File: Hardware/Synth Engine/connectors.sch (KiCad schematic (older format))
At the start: 8 parts, among them J10 Conn_01x13, J11 Conn_01x13, J13 Conn_01x05, J14 Conn_01x05, J15 Conn_01x05, J16 Conn_01x05, J8 Conn_01x13, J9 Conn_01x13

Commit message: fix LFO connector schem
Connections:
- net labels added: lfo_in_1, lfo_in_2, lfo_in_3, lfo_in_4, lfo_out_1, lfo_out_2, lfo_out_3, lfo_out_4
- wire segments 96 -> 104
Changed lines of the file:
@@
 	-1   0    0    -1
 $EndComp
+Text Label 3800 1450 0    60   ~ 0
+lfo_in_1
+Text Label 3800 1550 0    60   ~ 0
+lfo_out_1
+Text Label 3800 2150 0    60   ~ 0
+lfo_in_2
+Text Label 3800 2250 0    60   ~ 0
+lfo_out_2
+Text Label 3800 2800 0    60   ~ 0
+lfo_in_3
+Text Label 3800 2900 0    60   ~ 0
+lfo_out_3
+Text Label 3800 3450 0    60   ~ 0
+lfo_in_4
+Text Label 3800 3550 0    60   ~ 0
+lfo_out_4
+Text Label 8050 5650 2    60   ~ 0
+lfo_in_1
+Text Label 8050 5750 2    60   ~ 0
+lfo_out_1
+Text Label 8050 5850 2    60   ~ 0
+lfo_in_2
+Text Label 8050 5950 2    60   ~ 0
+lfo_out_2
+Text Label 8050 6050 2    60   ~ 0
+lfo_in_3
+Text Label 8050 6150 2    60   ~ 0
+lfo_out_3
+Text Label 8050 6250 2    60   ~ 0
+lfo_in_4
+Text Label 8050 6350 2    60   ~ 0
+lfo_out_4
+Text HLabel 8250 5650 2    60   Output ~ 0
+lfo_in_1
+Text HLabel 8250 5750 2    60   Input ~ 0
+lfo_out_1
+Text HLabel 8250 5850 2    60   Output ~ 0
+lfo_in_2
+Text HLabel 8250 5950 2    60   Input ~ 0
+lfo_out_2
+Text HLabel 8250 6050 2    60   Output ~ 0
+lfo_in_3
+Text HLabel 8250 6150 2    60   Input ~ 0
+lfo_out_3
+Text HLabel 8250 6250 2    60   Output ~ 0
+lfo_in_4
+Text HLabel 8250 6350 2    60   Input ~ 0
+lfo_out_4
+Wire Wire Line
+	8050 5650 8250 5650
+Wire Wire Line
+	8050 5750 8250 5750
+Wire Wire Line
+	8250 5850 8050 5850
+Wire Wire Line
+	8050 5950 8250 5950
+Wire Wire Line
+	8250 6050 8050 6050
+Wire Wire Line
+	8050 6150 8250 6150
+Wire Wire Line
+	8250 6250 8050 6250
+Wire Wire Line
+	8050 6350 8250 6350
 $EndSCHEMATC

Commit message: redo connector routing with 2-row connectors
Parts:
- removed J10, J11, J8, J9: Conn_01x13, Pin_Headers:Pin_Header_Straight_1x13_Pitch2.54mm, symbol Conn_01x13
- added J8, J9: Conn_02x12_Odd_Even, Pin_Headers:Pin_Header_Straight_2x12_Pitch2.54mm, symbol Conn_02x12_Odd_Even
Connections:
- wire segments 104 -> 100
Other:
- moved on the sheet: J13, J14, J15, J16

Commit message: add quantization again, fix connectors again, add mounting holes to main board
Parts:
- removed J8, J9: Conn_02x12_Odd_Even, Pin_Headers:Pin_Header_Straight_2x12_Pitch2.54mm, symbol Conn_02x12_Odd_Even
- added J8, J9: Conn_02x13_Odd_Even, Pin_Headers:Pin_Header_Straight_2x13_Pitch2.54mm, symbol Conn_02x13_Odd_Even
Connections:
- wire segments 100 -> 104

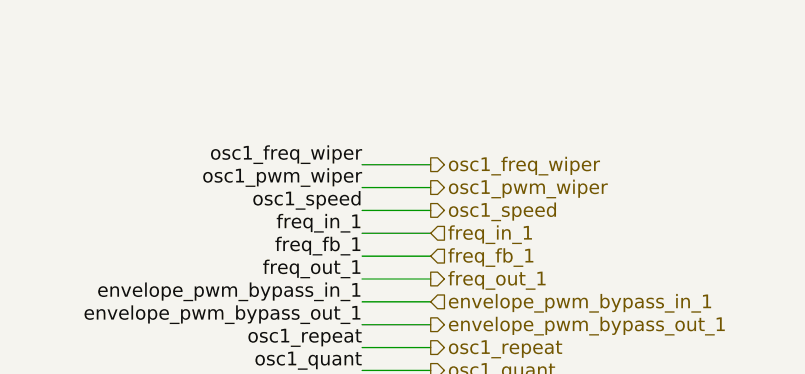
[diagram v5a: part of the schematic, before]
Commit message: redo second connector on main board
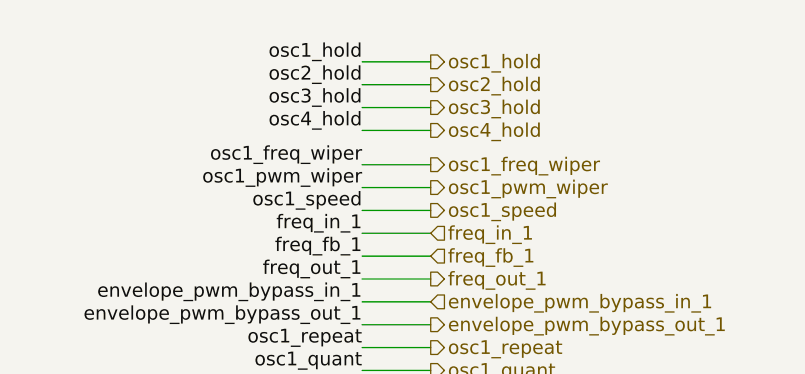
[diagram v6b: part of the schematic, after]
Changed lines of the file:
@@
 freq_out_4
 $Comp
-L +5V #PWR0115
+L +5V #PWR0109
 U 1 1 5C5CBE8C
 P 1900 750
-F 0 "#PWR0115" H 1900 600 50  0001 C CNN
+F 0 "#PWR0109" H 1900 600 50  0001 C CNN
 F 1 "+5V" H 1900 890 50  0000 C CNN
 F 2 "" H 1900 750 50  0001 C CNN
@@
 $EndComp
 $Comp
-L +5V #PWR0116
+L +5V #PWR0110
 U 1 1 5C5CBFC0
 P 2850 750
-F 0 "#PWR0116" H 2850 600 50  0001 C CNN
+F 0 "#PWR0110" H 2850 600 50  0001 C CNN
 F 1 "+5V" H 2850 890 50  0000 C CNN
 F 2 "" H 2850 750 50  0001 C CNN
@@
 $EndComp
 $Comp
-L +5V #PWR0117
+L +5V #PWR0111
 U 1 1 5C5CC0B3
 P 1900 2850
-F 0 "#PWR0117" H 1900 2700 50  0001 C CNN
+F 0 "#PWR0111" H 1900 2700 50  0001 C CNN
 F 1 "+5V" H 1900 2990 50  0000 C CNN
 F 2 "" H 1900 2850 50  0001 C CNN
@@
 $EndComp
 $Comp
-L +5V #PWR0118
+L +5V #PWR0112
 U 1 1 5C5CC16C
 P 2800 2850
-F 0 "#PWR0118" H 2800 2700 50  0001 C CNN
+F 0 "#PWR0112" H 2800 2700 50  0001 C CNN
 F 1 "+5V" H 2800 2990 50  0000 C CNN
 F 2 "" H 2800 2850 50  0001 C CNN
@@
 $EndComp
 $Comp
-L GND #PWR0119
+L GND #PWR0113
 U 1 1 5C5CC347
 P 1900 1900
-F 0 "#PWR0119" H 1900 1650 50  0001 C CNN
+F 0 "#PWR0113" H 1900 1650 50  0001 C CNN
 F 1 "GND" H 1900 1750 50  0000 C CNN
 F 2 "" H 1900 1900 50  0001 C CNN
@@
 $EndComp
 $Comp
-L GND #PWR0120
+L GND #PWR0114
 U 1 1 5C5CC7AC
 P 2850 1900
-F 0 "#PWR0120" H 2850 1650 50  0001 C CNN
+F 0 "#PWR0114" H 2850 1650 50  0001 C CNN
 F 1 "GND" H 2850 1750 50  0000 C CNN
 F 2 "" H 2850 1900 50  0001 C CNN
@@
 $EndComp
 $Comp
-L GND #PWR0121
+L GND #PWR0115
 U 1 1 5C5CC9CC
 P 1900 4000
-F 0 "#PWR0121" H 1900 3750 50  0001 C CNN
+F 0 "#PWR0115" H 1900 3750 50  0001 C CNN
 F 1 "GND" H 1900 3850 50  0000 C CNN
 F 2 "" H 1900 4000 50  0001 C CNN
@@
 $EndComp
 $Comp
-L GND #PWR0122
+L GND #PWR0116
 U 1 1 5C5CCA12
 P 2800 4000
-F 0 "#PWR0122" H 2800 3750 50  0001 C CNN
+F 0 "#PWR0116" H 2800 3750 50  0001 C CNN
 F 1 "GND" H 2800 3850 50  0000 C CNN
 F 2 "" H 2800 4000 50  0001 C CNN
@@
 	8300 4850 8000 4850
 $Comp
-L +5V #PWR0123
+L +5V #PWR0117
 U 1 1 5C63883F
 P 1900 1000
-F 0 "#PWR0123" H 1900 850 50  0001 C CNN
+F 0 "#PWR0117" H 1900 850 50  0001 C CNN
 F 1 "+5V" H 1900 1140 50  0000 C CNN
 F 2 "" H 1900 1000 50  0001 C CNN
@@
 $EndComp
 $Comp
-L +5V #PWR0124
+L +5V #PWR0118
 U 1 1 5C63885A
 P 1900 1200
-F 0 "#PWR0124" H 1900 1050 50  0001 C CNN
+F 0 "#PWR0118" H 1900 1050 50  0001 C CNN
 F 1 "+5V" H 1900 1340 50  0000 C CNN
 F 2 "" H 1900 1200 50  0001 C CNN
@@
 osc1_hold
 $Comp
-L GND #PWR0125
+L GND #PWR0119
 U 1 1 5C6388C2
 P 1900 2000
-F 0 "#PWR0125" H 1900 1750 50  0001 C CNN
+F 0 "#PWR0119" H 1900 1750 50  0001 C CNN
 F 1 "GND" H 1900 1850 50  0000 C CNN
 F 2 "" H 1900 2000 50  0001 C CNN
@@
 $EndComp
 $Comp
-L +5V #PWR0126
+L +5V #PWR0120
 U 1 1 5C638972
 P 2850 1000
-F 0 "#PWR0126" H 2850 850 50  0001 C CNN
+F 0 "#PWR0120" H 2850 850 50  0001 C CNN
 F 1 "+5V" H 2850 1140 50  0000 C CNN
 F 2 "" H 2850 1000 50  0001 C CNN
@@
 $EndComp
 $Comp
-L +5V #PWR0127
+L +5V #PWR0121
 U 1 1 5C63898D
 P 2850 1200
-F 0 "#PWR0127" H 2850 1050 50  0001 C CNN
+F 0 "#PWR0121" H 2850 1050 50  0001 C CNN
 F 1 "+5V" H 2850 1340 50  0000 C CNN
 F 2 "" H 2850 1200 50  0001 C CNN
@@
 osc2_hold
 $Comp
-L GND #PWR0128
+L GND #PWR0122
 U 1 1 5C6389D7
 P 2850 2000
-F 0 "#PWR0128" H 2850 1750 50  0001 C CNN
+F 0 "#PWR0122" H 2850 1750 50  0001 C CNN
 F 1 "GND" H 2850 1850 50  0000 C CNN
 F 2 "" H 2850 2000 50  0001 C CNN
@@
 $EndComp
 $Comp
-L +5V #PWR0129
+L +5V #PWR0123
 U 1 1 5C638A27
 P 1900 3100
-F 0 "#PWR0129" H 1900 2950 50  0001 C CNN
+F 0 "#PWR0123" H 1900 2950 50  0001 C CNN
 F 1 "+5V" H 1900 3240 50  0000 C CNN
 F 2 "" H 1900 3100 50  0001 C CNN
@@
 $EndComp
 $Comp
-L +5V #PWR0130
+L +5V #PWR0124
 U 1 1 5C638A9A
 P 1900 3300
-F 0 "#PWR0130" H 1900 3150 50  0001 C CNN
+F 0 "#PWR0124" H 1900 3150 50  0001 C CNN
 F 1 "+5V" H 1900 3440 50  0000 C CNN
 F 2 "" H 1900 3300 50  0001 C CNN
@@
 osc3_hold
 $Comp
-L GND #PWR0131
+L GND #PWR0125
 U 1 1 5C638ADC
 P 1900 4100
-F 0 "#PWR0131" H 1900 3850 50  0001 C CNN
+F 0 "#PWR0125" H 1900 3850 50  0001 C CNN
 F 1 "GND" H 1900 3950 50  0000 C CNN
 F 2 "" H 1900 4100 50  0001 C CNN
@@
 $EndComp
 $Comp
-L +5V #PWR0132
+L +5V #PWR0126
 U 1 1 5C638BD0
 P 2800 3100
-F 0 "#PWR0132" H 2800 2950 50  0001 C CNN
+F 0 "#PWR0126" H 2800 2950 50  0001 C CNN
 F 1 "+5V" H 2800 3240 50  0000 C CNN
 F 2 "" H 2800 3100 50  0001 C CNN
@@
 $EndComp
 $Comp
-L +5V #PWR0133
+L +5V #PWR0127
 U 1 1 5C638BE7
 P 2800 3300
-F 0 "#PWR0133" H 2800 3150 50  0001 C CNN
+F 0 "#PWR0127" H 2800 3150 50  0001 C CNN
 F 1 "+5V" H 2800 3440 50  0000 C CNN
 F 2 "" H 2800 3300 50  0001 C CNN
@@
 osc4_hold
 $Comp
-L GND #PWR0134
+L GND #PWR0128
 U 1 1 5C638C2E
 P 2800 4100
-F 0 "#PWR0134" H 2800 3850 50  0001 C CNN
+F 0 "#PWR0128" H 2800 3850 50  0001 C CNN
 F 1 "GND" H 2800 3950 50  0000 C CNN
 F 2 "" H 2800 4100 50  0001 C CNN
@@
 	1    0    0    -1
 $EndComp
+Text HLabel 8300 750  2    60   Output ~ 0
+osc1_hold
+Text HLabel 8300 850  2    60   Output ~ 0
+osc2_hold
+Text HLabel 8300 950  2    60   Output ~ 0
+osc3_hold
+Text HLabel 8300 1050 2    60   Output ~ 0
+osc4_hold
+Text Label 8000 750  2    60   ~ 0
+osc1_hold
+Wire Wire Line
+	8300 750  8000 750
+Text Label 8000 850  2    60   ~ 0
+osc2_hold
+Text Label 8000 950  2    60   ~ 0
+osc3_hold
+Text Label 8000 1050 2    60   ~ 0
+osc4_hold
+Wire Wire Line
+	8000 850  8300 850
+Wire Wire Line
+	8300 950  8000 950
+Wire Wire Line
+	8000 1050 8300 1050
 $EndSCHEMATC
